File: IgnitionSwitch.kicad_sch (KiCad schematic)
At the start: 13 parts, among them J28 KILL_SW_IND, J7 BPS_PWR_OUT, J9 POW_2ND_CONN, SW8 SW_Rotary2x6, U5 EL3H7, U6 EL3H7

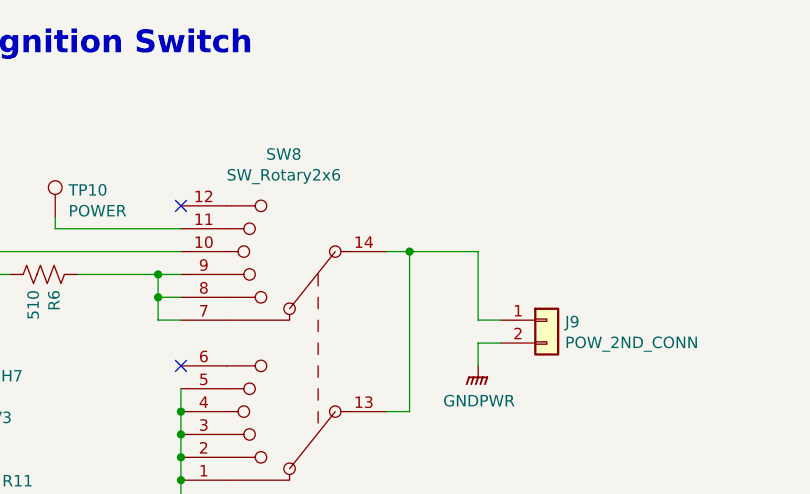
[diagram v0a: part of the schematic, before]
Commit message: removed camera, fixed connectors, and changed status LEDS
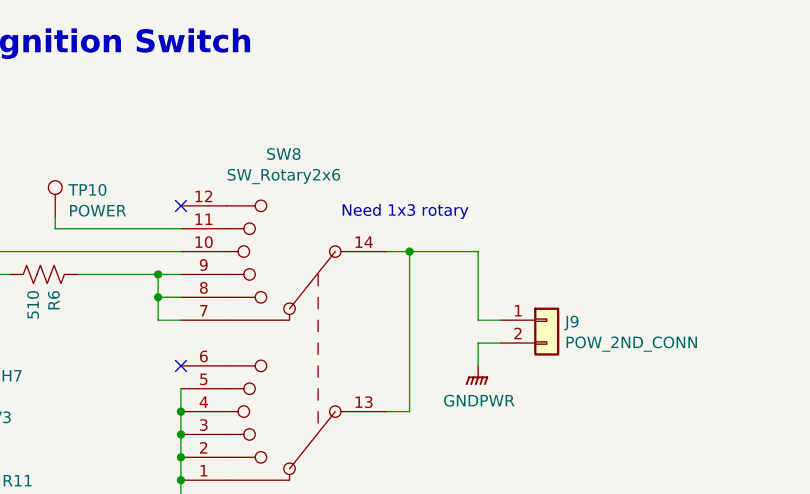
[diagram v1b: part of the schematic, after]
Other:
- note added: "Need 1x3 rotary"
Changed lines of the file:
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@@
+		)
+	)
+	(text "Need 1x3 rotary"
+		(exclude_from_sim no)
+		(at 176.022 82.042 0)
+		(effects
+			(font
+				(size 1.27 1.27)
+				(color 255 0 7 1)
+			)
 		)
 	)

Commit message: Schematic finished :) hopefully not broken
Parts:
- removed J7: BPS_PWR_OUT, UTSVT_Connectors:Molex_MicroFit3.0_1x2xP3.00mm_PolarizingPeg_Vertical, symbol Connector_Generic:Conn_01x02
- removed SW8: SW_Rotary2x6, Connector_Molex:Molex_Micro-Fit_3.0_43045-1412_2x07_P3.00mm_Vertical, symbol Switch:SW_Rotary2x6
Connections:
- no-connect marks 2 -> 1
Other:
- note removed: "TODO: This connector was originally the other way around. Will this still connect?"
